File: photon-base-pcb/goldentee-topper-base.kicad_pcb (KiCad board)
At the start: 2 copper layers, 208 x 108 mm, 79 parts, among them M1 photon_module, P1 CONN_01X04, P2 CONN_01X16, Q1 Q_NMOS_DGS, Q10 Q_PMOS_SDGD, Q11 Q_NMOS_DGS, Q12 Q_PMOS_SDGD, Q13 Q_NMOS_DGS, Q14 Q_PMOS_SDGD, Q2 Q_PMOS_SDGD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

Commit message: first concept layout
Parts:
- removed D1, D2, D3, D4, D5, D6, D7: LED, LEDs:LED_0603
- removed R10, R11, R13, R14, R15, R16, R9: 47K, Resistors_SMD:R_0603_HandSoldering
- removed R17, R2, R25, R27, R4, R6, R8: 4.7K, Resistors_SMD:R_0603_HandSoldering
- Q10, Q12, Q14, Q2, Q4, Q6, Q8: value Q_PMOS_SDGD -> Q_PMOS_GDS; footprint TO_SOT_Packages_SMD:SOT-223 -> TO_SOT_Packages_SMD:TO-252-2Lead
- moved U3 46.1 mm to (190.5, 94.9)
- moved C3 46.1 mm to (197.9, 104.3)
- moved C4 46.1 mm to (183.4, 104.3)
- moved C5 46.1 mm to (197.9, 95.1)
- moved C6 46.1 mm to (183.4, 95.1)
- moved U1 46.1 mm to (190.4, 104.3)
- moved R18 20.9 mm to (240.7, 114.3), turned to 180 degrees
- moved R19 18.6 mm to (240.7, 116.8), turned to 180 degrees
- moved R24 18.4 mm to (240.7, 127.0), turned to 180 degrees
- moved R20 18.0 mm to (240.7, 119.4), turned to 180 degrees
- moved R23 17.8 mm to (240.7, 124.5), turned to 180 degrees
- moved R22 17.5 mm to (240.7, 121.9), turned to 180 degrees
- moved P1 14.8 mm to (233.7, 149.1)
- moved C7 12.3 mm to (225.9, 133.5)
- moved C8 12.3 mm to (230.9, 133.5)
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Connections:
- M1 pad 13: /ROW_1_8_SW -> /ROW_5_12_SW
- M1 pad 14: /ROW_2_9_SW -> /ROW_7_14_SW
- M1 pad 15: /ROW_3_10_SW -> /ROW_4_11_SW
- M1 pad 16: /ROW_4_11_SW -> /ROW_6_13_SW
- M1 pad 17: /ROW_5_12_SW -> /ROW_3_10_SW
- M1 pad 18: /ROW_6_13_SW -> /ROW_1_8_SW
- M1 pad 19: /ROW_7_14_SW -> /ROW_2_9_SW
- Q10 pad 1: +12V -> Net-(Q10-Pad1)
- Q10 pad 3: Net-(Q10-Pad3) -> +12V
- Q12 pad 1: +12V -> Net-(Q11-Pad1)
- Q12 pad 3: Net-(Q11-Pad1) -> +12V
- Q14 pad 1: +12V -> Net-(Q13-Pad1)
- Q14 pad 3: Net-(Q13-Pad1) -> +12V
- Q2 pad 1: +12V -> Net-(Q1-Pad1)
- Q2 pad 3: Net-(Q1-Pad1) -> +12V
- Q4 pad 1: +12V -> Net-(Q3-Pad1)
- Q4 pad 3: Net-(Q3-Pad1) -> +12V
- Q6 pad 1: +12V -> Net-(Q5-Pad1)
- Q6 pad 3: Net-(Q5-Pad1) -> +12V
- Q8 pad 1: +12V -> Net-(Q7-Pad1)
- Q8 pad 3: Net-(Q7-Pad1) -> +12V
- Q9 pad 1: Net-(Q10-Pad3) -> Net-(Q10-Pad1)
- R12 pad 2: Net-(Q10-Pad3) -> Net-(Q10-Pad1)
- R29 pad 2: /ROW_7_14_SW -> /ROW_2_9_SW
- R31 pad 2: /ROW_6_13_SW -> /ROW_1_8_SW
- R33 pad 2: /ROW_5_12_SW -> /ROW_3_10_SW
- R35 pad 2: /ROW_4_11_SW -> /ROW_6_13_SW
- R37 pad 2: /ROW_3_10_SW -> /ROW_4_11_SW
- R39 pad 2: /ROW_2_9_SW -> /ROW_7_14_SW
- R40 pad 2: /ROW_1_8_SW -> /ROW_5_12_SW
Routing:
- net +12V: track 0.00 -> 253.2 mm
- net /ROW_2_9_SW: track 0.00 -> 97.1 mm
- net /ROW_1_8_SW: track 0.00 -> 90.8 mm, vias 0 -> 2
- net /ROW_3_10_SW: track 0.00 -> 85.1 mm, vias 0 -> 2
- net /ROW_6_13_SW: track 0.00 -> 78.7 mm, vias 0 -> 2
- net /ROW_4_11_SW: track 0.00 -> 72.9 mm, vias 0 -> 2
- net /ROW_7_14_SW: track 0.00 -> 66.0 mm, vias 0 -> 2
- net /ROW_5_12_SW: track 0.00 -> 59.7 mm, vias 0 -> 2
- net /BOTTOM_CLK_5V: track 0.32 -> 33.1 mm
- net /#OUTPUT_ON_5V: track 0.32 -> 32.6 mm
- net /BOTTOM_DATA_5V: track 0.32 -> 30.7 mm
- net /RCK_ALL_5V: track 0.00 -> 30.3 mm
- net /TOP_DATA_5V: track 0.00 -> 30.1 mm
- net GND: track 0.00 -> 18.5 mm, vias 0 -> 10
- net /TOP_CLK_5V: track 0.00 -> 17.7 mm
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- added copper zone on B.Cu, net GND
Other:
- net class Default: clearance 0.2 -> 0.25
- net class LED_POWER: clearance 0.2 -> 0.25; trace_width 2.5 -> 3; via_dia 0.6 -> 3; via_drill 0.4 -> 1
- rule trace_clearance: 0.2 -> 0.25

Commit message: Small Square pcb, silk yet to be arranged.
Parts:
- removed C5, C6: 10uF 25V, Capacitors_SMD:C_1210_HandSoldering
- removed R28: 47K, Resistors_SMD:R_0603_HandSoldering
- removed U3: NCP1117ST33T3G, TO_SOT_Packages_SMD:SOT-223
- added R2: 47K, Resistors_SMD:R_0603_HandSoldering, F.Cu at (222.4, 56.0)
- added REF**: MountingHole_6mm, Mounting_Holes:MountingHole_6mm, F.Cu at (180.0, 153.0)
- added REF**: MountingHole_6mm, Mounting_Holes:MountingHole_6mm, F.Cu at (180.0, 55.5)
- added REF**: MountingHole_6mm, Mounting_Holes:MountingHole_6mm, F.Cu at (253.0, 55.5)
- added REF**: MountingHole_6mm, Mounting_Holes:MountingHole_6mm, F.Cu at (253.0, 153.0)
- U1: value NCP1117ST50T3G -> NCP1117
- moved R38 94.2 mm to (222.4, 64.4), turned to 270 degrees
- moved R36 84.4 mm to (222.4, 72.8), turned to 270 degrees
- moved M1 75.7 mm to (199.4, 65.2), turned to 180 degrees
- moved R34 74.8 mm to (222.4, 81.2), turned to 270 degrees
- moved R32 65.6 mm to (222.4, 89.6), turned to 270 degrees
- moved R30 57.0 mm to (222.4, 98.0), turned to 270 degrees
- moved R40 48.3 mm to (222.4, 106.4), turned to 270 degrees
- moved R19 39.0 mm to (202.0, 111.6), turned to 0 degrees
- moved R18 38.9 mm to (202.0, 109.6), turned to 0 degrees
- moved R22 38.5 mm to (202.2, 119.4), turned to 0 degrees
- moved R20 38.5 mm to (202.2, 117.4), turned to 0 degrees
- moved R23 38.4 mm to (202.2, 125.4), turned to 0 degrees
- moved R24 38.4 mm to (202.2, 127.4), turned to 0 degrees
- moved R31 36.5 mm to (189.0, 111.6), turned to 0 degrees
- moved R29 36.1 mm to (189.0, 109.6), turned to 0 degrees
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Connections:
- M1 pad 10: /#OUTPUT_ON_3V3 -> /ROW_3_10_SW
- M1 pad 11: /RCK_ALL_3V3 -> /ROW_1_8_SW
- M1 pad 12: (no net) -> /ROW_2_9_SW
- M1 pad 13: /ROW_5_12_SW -> (no net)
- M1 pad 14: /ROW_7_14_SW -> /TOP_CLK_3V3
- M1 pad 15: /ROW_4_11_SW -> /BOTTOM_CLK_3V3
- M1 pad 16: /ROW_6_13_SW -> /TOP_DATA_3V3
- M1 pad 17: /ROW_3_10_SW -> /BOTTOM_DATA_3V3
- M1 pad 18: /ROW_1_8_SW -> /RCK_ALL_3V3
- M1 pad 19: /ROW_2_9_SW -> /#OUTPUT_ON_3V3
- M1 pad 24: Net-(M1-Pad24) -> +3V3
- M1 pad 6: (no net) -> /ROW_5_12_SW
- M1 pad 7: /BOTTOM_DATA_3V3 -> /ROW_7_14_SW
- M1 pad 8: /TOP_DATA_3V3 -> /ROW_4_11_SW
- M1 pad 9: /LED_CLK_3V3 -> /ROW_6_13_SW
- P1 pad 1: GND -> /LED_GND
- P1 pad 2: +12V -> /LED_PWR
- P2 pad 13: GND -> /LED_GND
- Q10 pad 3: +12V -> /LED_PWR
- Q12 pad 3: +12V -> /LED_PWR
- Q14 pad 3: +12V -> /LED_PWR
- Q2 pad 3: +12V -> /LED_PWR
- Q4 pad 3: +12V -> /LED_PWR
- Q6 pad 3: +12V -> /LED_PWR
- Q8 pad 3: +12V -> /LED_PWR
- R1 pad 1: +12V -> /LED_PWR
- R12 pad 1: +12V -> /LED_PWR
- R21 pad 1: +12V -> /LED_PWR
- R26 pad 1: +12V -> /LED_PWR
- R29 pad 2: /ROW_2_9_SW -> /#OUTPUT_ON_3V3
- R3 pad 1: +12V -> /LED_PWR
- R30 pad 1: /BOTTOM_DATA_3V3 -> /ROW_7_14_SW
- R31 pad 2: /ROW_1_8_SW -> /RCK_ALL_3V3
- R32 pad 1: /TOP_DATA_3V3 -> /ROW_4_11_SW
- R33 pad 2: /ROW_3_10_SW -> /BOTTOM_DATA_3V3
- R34 pad 1: /LED_CLK_3V3 -> /ROW_6_13_SW
- R35 pad 2: /ROW_6_13_SW -> /TOP_DATA_3V3
- R36 pad 1: /#OUTPUT_ON_3V3 -> /ROW_3_10_SW
- R37 pad 2: /ROW_4_11_SW -> /BOTTOM_CLK_3V3
- R38 pad 1: /RCK_ALL_3V3 -> /ROW_1_8_SW
- R39 pad 2: /ROW_7_14_SW -> /TOP_CLK_3V3
- R40 pad 1: GND -> /ROW_5_12_SW
- R40 pad 2: /ROW_5_12_SW -> GND
- R5 pad 1: +12V -> /LED_PWR
- R7 pad 1: +12V -> /LED_PWR
- U1 pad 4: (no net) -> +5V
- U4 pad 2: /LED_CLK_3V3 -> /BOTTOM_CLK_3V3
- U4 pad 3: /LED_CLK_3V3 -> /TOP_CLK_3V3
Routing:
- net /LED_PWR: track 0.00 -> 208.9 mm
- net +12V: track 253.2 -> 113.8 mm
- net /TOP_CLK_3V3: track 0.00 -> 81.3 mm
- net /ROW_2_9_SW: track 97.1 -> 17.1 mm, vias 0 -> 1
- net GND: track 18.5 -> 94.8 mm, vias 10 -> 15
- net /BOTTOM_CLK_3V3: track 0.00 -> 76.2 mm
- net +3V3: track 0.00 -> 74.0 mm, vias 0 -> 4
- net /ROW_1_8_SW: track 90.8 -> 23.6 mm, vias 2 -> 1
- net /TOP_DATA_3V3: track 0.00 -> 67.0 mm
- net /ROW_3_10_SW: track 85.1 -> 22.8 mm, vias 2 -> 1
- net /BOTTOM_DATA_3V3: track 0.00 -> 62.0 mm
- net +5V: track 0.00 -> 57.9 mm
- net /RCK_ALL_3V3: track 0.00 -> 52.9 mm
- net /ROW_6_13_SW: track 78.7 -> 29.8 mm, vias 2 -> 1
- net /#OUTPUT_ON_3V3: track 0.00 -> 48.9 mm
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- added copper zone on F.Cu, net +5V
- added copper zone on F.Cu, net GND
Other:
- board size 208 x 108 mm -> 83 x 108 mm
- net class 3V3_POWER added: clearance 0.25, trace_width 1, via_dia 0.7, via_drill 0.4
- net class Default: via_dia 0.6 -> 0.7
- net class LED_POWER: clearance 0.25 -> 0.5; trace_width 3 -> 2.5; via_dia 3 -> 2.5

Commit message: V3 Release
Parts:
- added P3: CONN_01X06, Pin_Headers:Pin_Header_Straight_1x06_Pitch2.54mm, F.Cu at (214.6, 72.6)
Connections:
- M1 pad 3: (no net) -> /UART_RXD
- M1 pad 4: (no net) -> /UART_TXD
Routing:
- net /UART_TXD: track 0.00 -> 10.1 mm
- net /UART_RXD: track 0.00 -> 10.1 mm
- net +5V: track 57.9 -> 64.2 mm

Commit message: fixed sideways nfets, relayed out the area around the new FET configuration. BOM updates for all the initial parts.  BOM reflects the fixed NFET pinout.
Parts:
- Q1, Q11, Q13, Q3, Q5, Q7, Q9: value Q_NMOS_DGS -> Q_NMOS_GSD
- moved P3 2.85 mm to (213.2, 70.2)
- moved R2 2.00 mm to (220.4, 56.0)
- moved R30 2.00 mm to (220.4, 98.0)
- moved R32 2.00 mm to (220.4, 89.6)
- moved R34 2.00 mm to (220.4, 81.2)
- moved R36 2.00 mm to (220.4, 72.8)
- moved R38 2.00 mm to (220.4, 64.4)
- moved R40 2.00 mm to (220.4, 106.4)
- moved Q13 1.21 mm to (224.2, 98.0), turned to 0 degrees
- moved Q5 1.17 mm to (224.2, 72.8), turned to 0 degrees
- moved Q7 1.17 mm to (224.2, 89.6), turned to 0 degrees
- moved Q3 1.17 mm to (224.2, 56.0), turned to 0 degrees
- moved Q1 1.17 mm to (224.2, 64.4), turned to 0 degrees
- moved Q11 1.17 mm to (224.2, 81.2), turned to 0 degrees
- moved Q9 1.17 mm to (224.2, 106.4), turned to 0 degrees
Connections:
- Q1 pad 1: Net-(Q1-Pad1) -> /ROW_1_8_SW
- Q1 pad 2: /ROW_1_8_SW -> GND
- Q1 pad 3: GND -> Net-(Q1-Pad3)
- Q11 pad 1: Net-(Q11-Pad1) -> /ROW_6_13_SW
- Q11 pad 2: /ROW_6_13_SW -> GND
- Q11 pad 3: GND -> Net-(Q11-Pad3)
- Q12 pad 1: Net-(Q11-Pad1) -> Net-(Q11-Pad3)
- Q13 pad 1: Net-(Q13-Pad1) -> /ROW_7_14_SW
- Q13 pad 2: /ROW_7_14_SW -> GND
- Q13 pad 3: GND -> Net-(Q13-Pad3)
- Q14 pad 1: Net-(Q13-Pad1) -> Net-(Q13-Pad3)
- Q2 pad 1: Net-(Q1-Pad1) -> Net-(Q1-Pad3)
- Q3 pad 1: Net-(Q3-Pad1) -> /ROW_2_9_SW
- Q3 pad 2: /ROW_2_9_SW -> GND
- Q3 pad 3: GND -> Net-(Q3-Pad3)
- Q4 pad 1: Net-(Q3-Pad1) -> Net-(Q3-Pad3)
- Q5 pad 1: Net-(Q5-Pad1) -> /ROW_3_10_SW
- Q5 pad 2: /ROW_3_10_SW -> GND
- Q5 pad 3: GND -> Net-(Q5-Pad3)
- Q6 pad 1: Net-(Q5-Pad1) -> Net-(Q5-Pad3)
- Q7 pad 1: Net-(Q7-Pad1) -> /ROW_4_11_SW
- Q7 pad 2: /ROW_4_11_SW -> GND
- Q7 pad 3: GND -> Net-(Q7-Pad3)
- Q8 pad 1: Net-(Q7-Pad1) -> Net-(Q7-Pad3)
- Q9 pad 1: Net-(Q10-Pad1) -> /ROW_5_12_SW
- Q9 pad 2: /ROW_5_12_SW -> GND
- Q9 pad 3: GND -> Net-(Q10-Pad1)
- R1 pad 2: Net-(Q1-Pad1) -> Net-(Q1-Pad3)
- R21 pad 2: Net-(Q11-Pad1) -> Net-(Q11-Pad3)
- R26 pad 2: Net-(Q13-Pad1) -> Net-(Q13-Pad3)
- R3 pad 2: Net-(Q3-Pad1) -> Net-(Q3-Pad3)
- R5 pad 2: Net-(Q5-Pad1) -> Net-(Q5-Pad3)
- R7 pad 2: Net-(Q7-Pad1) -> Net-(Q7-Pad3)
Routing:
- net GND: track 94.8 -> 102.6 mm, vias 15 -> 19
- net Net-(Q1-Pad3): track 0.00 -> 6.49 mm
- net Net-(Q11-Pad3): track 0.00 -> 6.49 mm
- net Net-(Q5-Pad3): track 0.00 -> 6.49 mm
- net Net-(Q3-Pad3): track 0.00 -> 6.49 mm
- net Net-(Q13-Pad3): track 0.00 -> 6.49 mm
- net Net-(Q7-Pad3): track 0.00 -> 6.49 mm
- net Net-(Q1-Pad1): track 5.29 -> 0.00 mm
- net Net-(Q7-Pad1): track 5.29 -> 0.00 mm
- net Net-(Q5-Pad1): track 5.29 -> 0.00 mm
- net Net-(Q3-Pad1): track 5.29 -> 0.00 mm
- net Net-(Q11-Pad1): track 5.29 -> 0.00 mm
- net Net-(Q13-Pad1): track 5.24 -> 0.00 mm
- net /ROW_2_9_SW: track 17.1 -> 21.9 mm
- net /ROW_4_11_SW: track 36.4 -> 40.9 mm
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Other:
- net class LED_POWER: clearance 0.5 -> 0.25; trace_width 2.5 -> 3.25

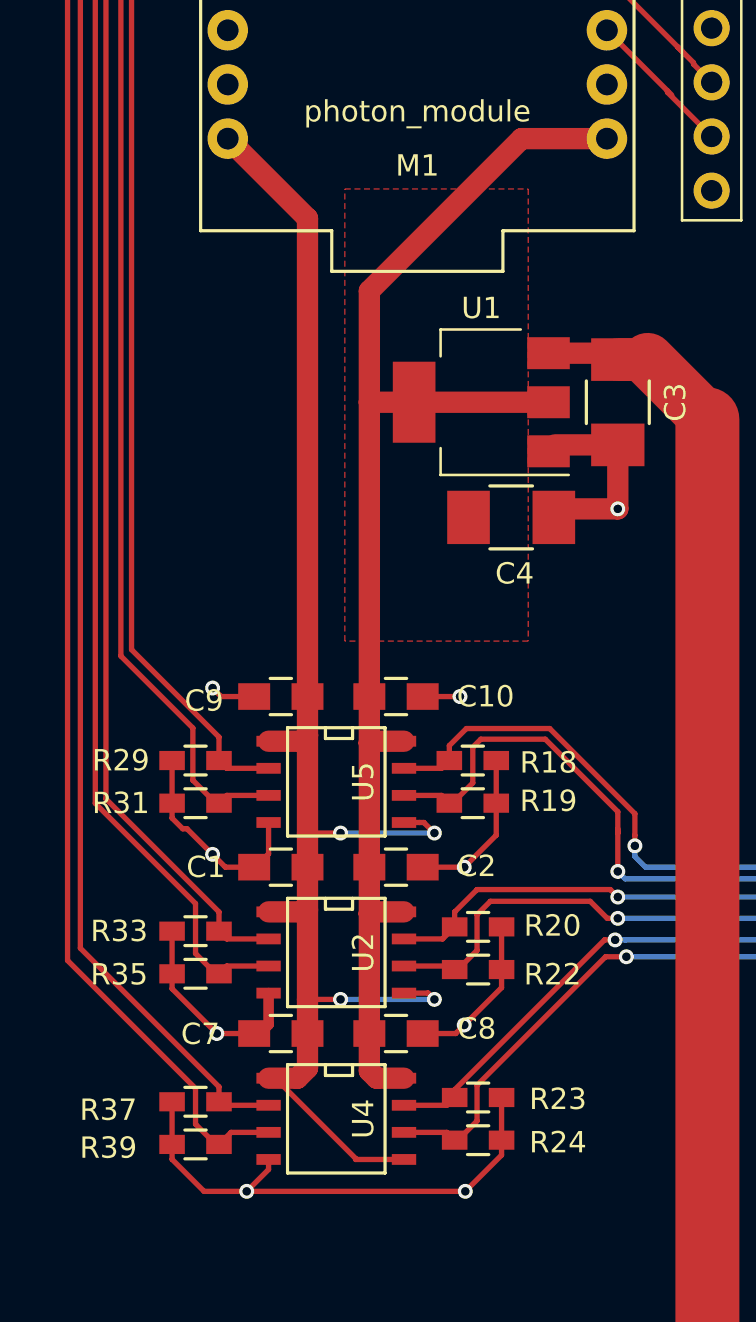
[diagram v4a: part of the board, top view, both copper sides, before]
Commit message: level shifter footprint update
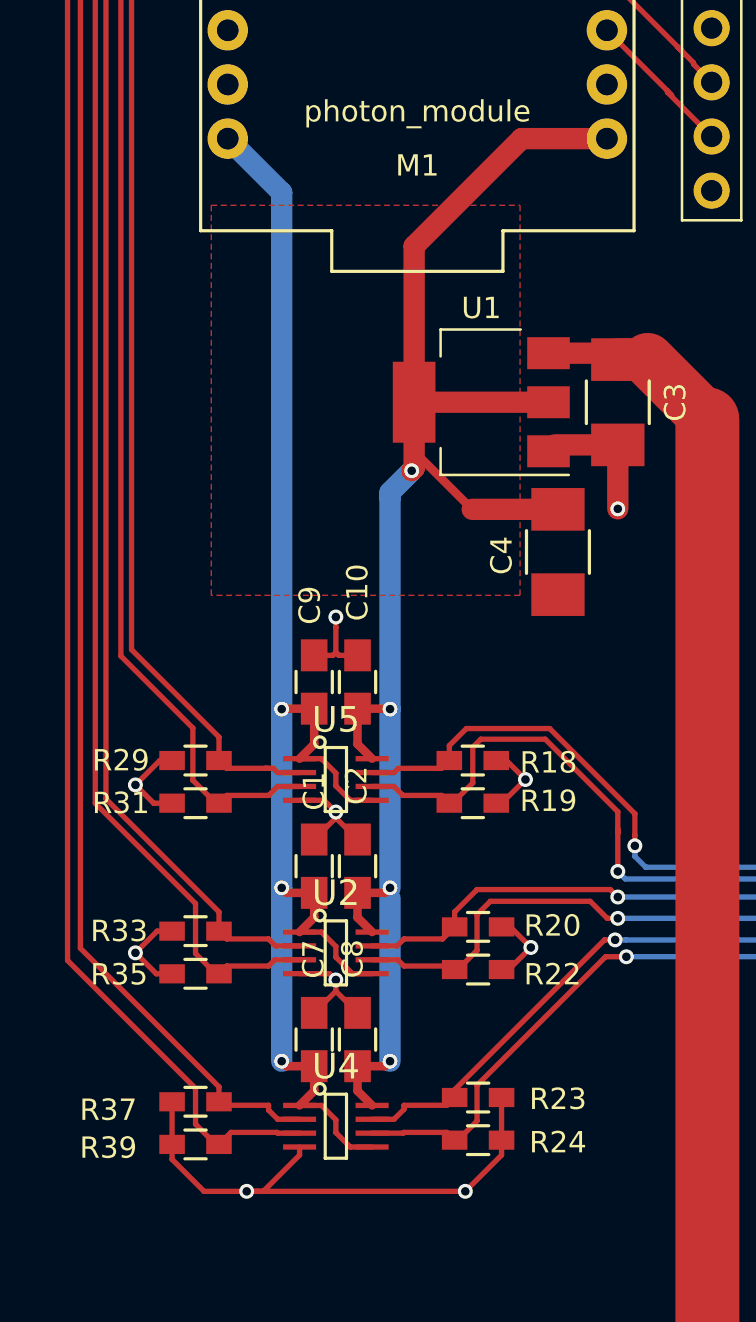
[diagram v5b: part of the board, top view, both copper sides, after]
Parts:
- U2, U4, U5: footprint SMD_Packages:SOIC-8-N -> goldentee_topper_base:SN74LVC2T45DCTR
- moved C4 2.73 mm to (206.0, 99.8), turned to 270 degrees
- moved C10 1.93 mm to (196.6, 105.9), turned to 90 degrees
- moved C8 1.83 mm to (196.6, 122.7), turned to 90 degrees
- moved C2 1.80 mm to (196.6, 114.6), turned to 90 degrees
- moved C9 1.71 mm to (194.6, 105.9), turned to 270 degrees
- moved C7 1.59 mm to (194.6, 122.7), turned to 270 degrees
- moved C1 1.56 mm to (194.6, 114.6), turned to 270 degrees
- moved U4 0.35 mm to (195.6, 126.7)
- moved U5 0.11 mm to (195.6, 110.5)
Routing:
- net +5V: track 64.2 -> 74.5 mm, vias 0 -> 4
- net GND: track 102.6 -> 92.6 mm, vias 19 -> 17
- net +3V3: track 74.0 -> 69.6 mm, vias 4 -> 3
- net /BOTTOM_CLK_5V: track 57.1 -> 59.0 mm
- net /BOTTOM_CLK_3V3: track 76.2 -> 78.1 mm
- net /#OUTPUT_ON_3V3: track 48.9 -> 50.6 mm
- net /RCK_ALL_5V: track 66.5 -> 68.2 mm
- net /BOTTOM_DATA_5V: track 58.2 -> 59.8 mm
- net /RCK_ALL_3V3: track 52.9 -> 54.6 mm
- net /TOP_DATA_5V: track 57.6 -> 59.3 mm
- net /BOTTOM_DATA_3V3: track 62.0 -> 63.6 mm
- net /#OUTPUT_ON_5V: track 67.8 -> 69.4 mm
- net /TOP_DATA_3V3: track 67.0 -> 68.6 mm
- net /TOP_CLK_5V: track 58.4 -> 59.9 mm
- net /TOP_CLK_3V3: track 81.3 -> 82.7 mm
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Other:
- net class 3V3_POWER: trace_width 1 -> 0.4
